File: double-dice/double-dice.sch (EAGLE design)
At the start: 3 parts, among them IC1 74HC595N, IC2 74HC595N

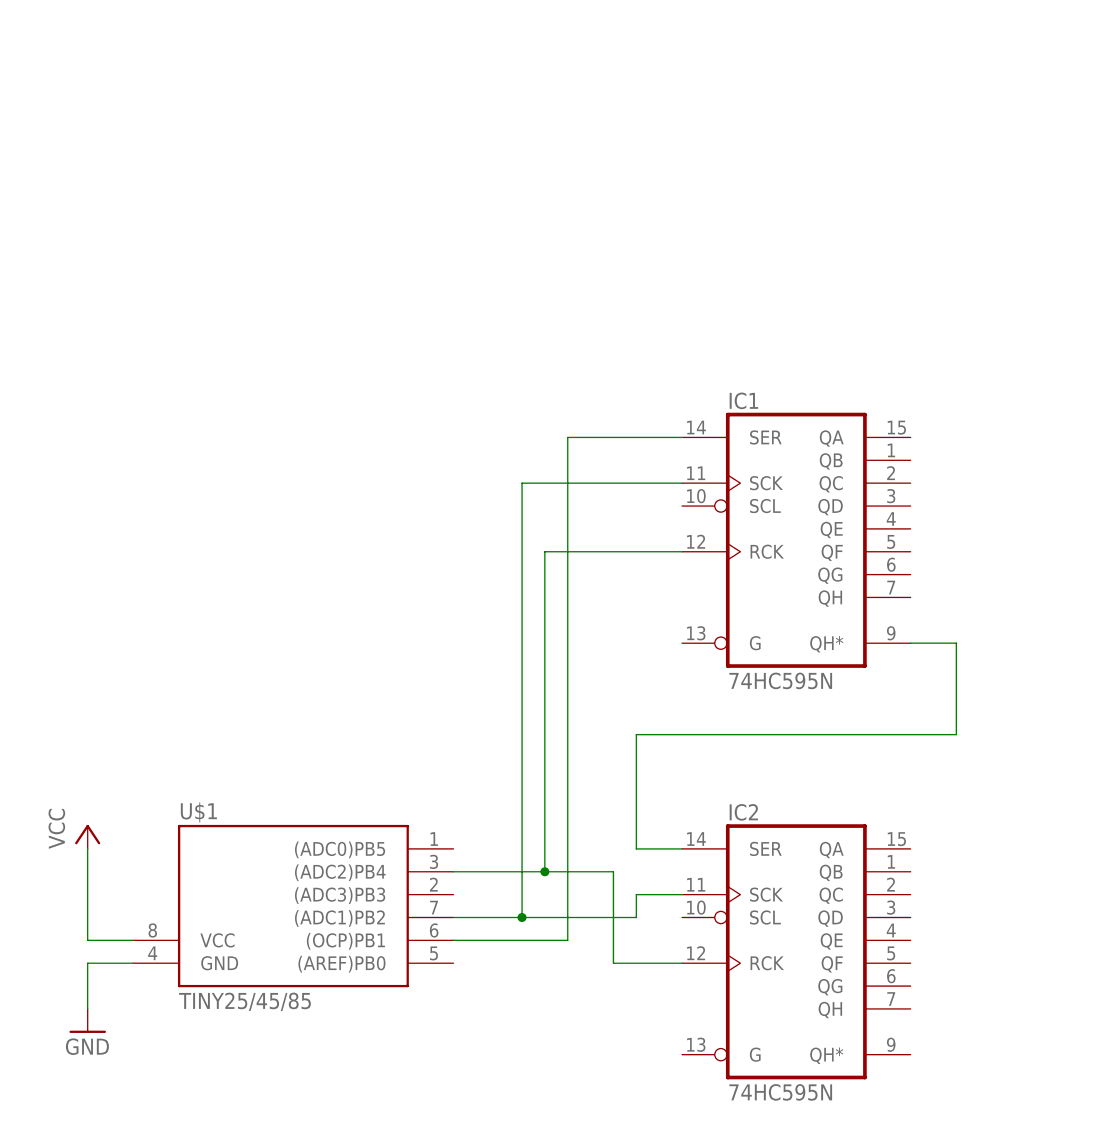
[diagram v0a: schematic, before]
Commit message: Added frame and connected SCL of the two 74595's
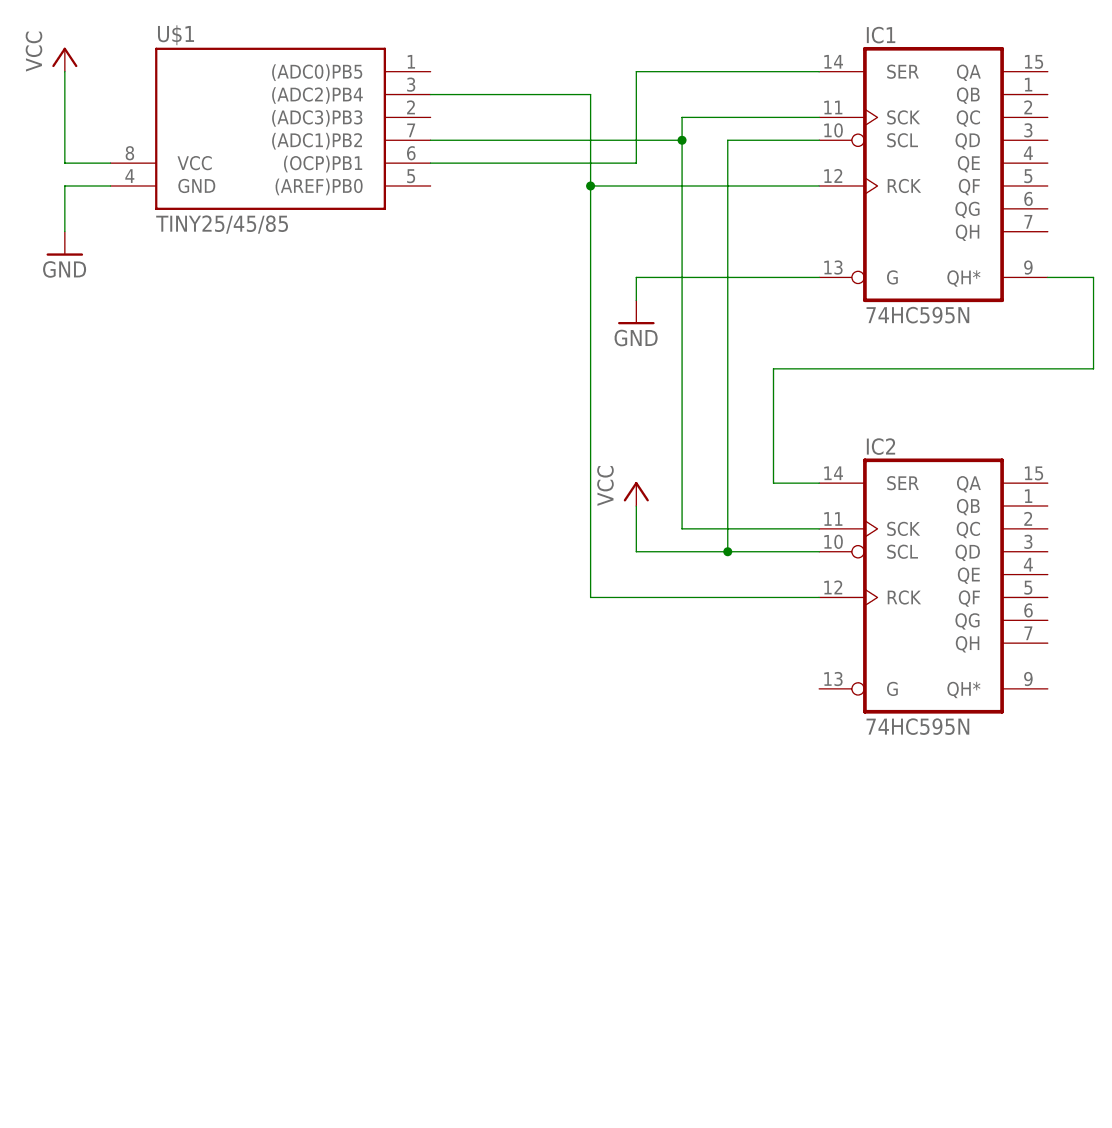
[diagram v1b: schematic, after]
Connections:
- net GND: now also IC1A.G
- net VCC: now also IC1A.SCL, IC2A.SCL
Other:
- moved on the sheet: IC1, IC2, U$1
